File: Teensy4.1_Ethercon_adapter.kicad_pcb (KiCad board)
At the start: 2 copper layers, 20 x 32 mm, 10 parts, among them J1 Conn_01x06, J2 NE8FAV

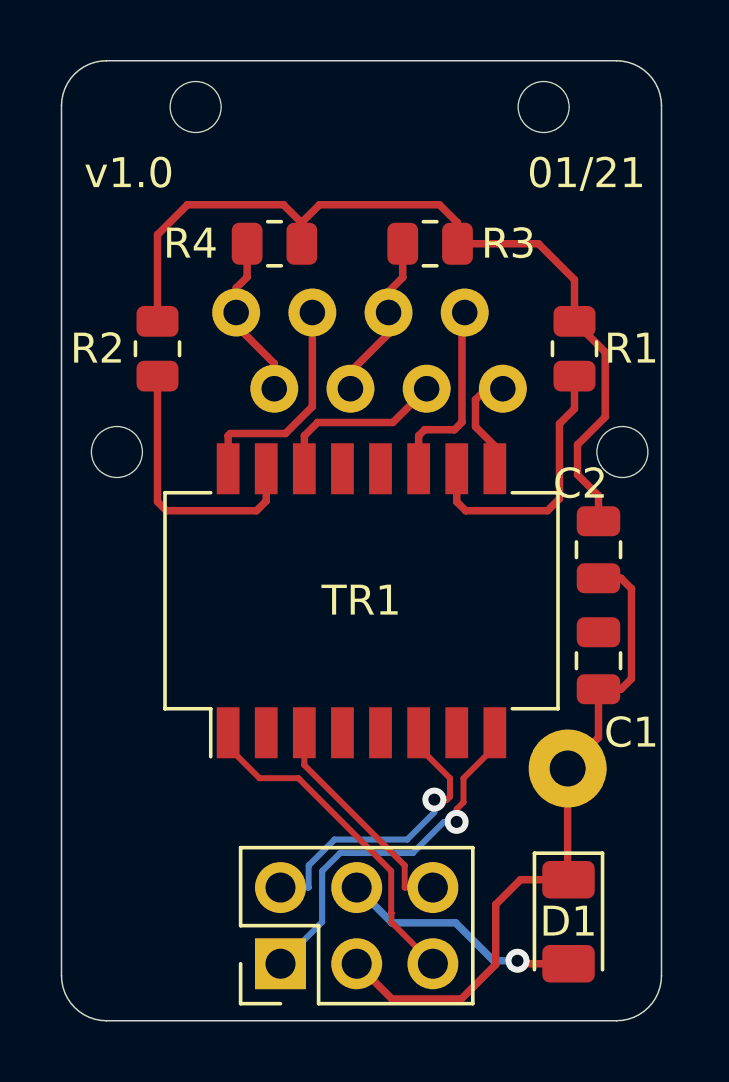
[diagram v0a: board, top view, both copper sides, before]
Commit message: Version 1.1 - fixed routing and pin header pitch (2mm)
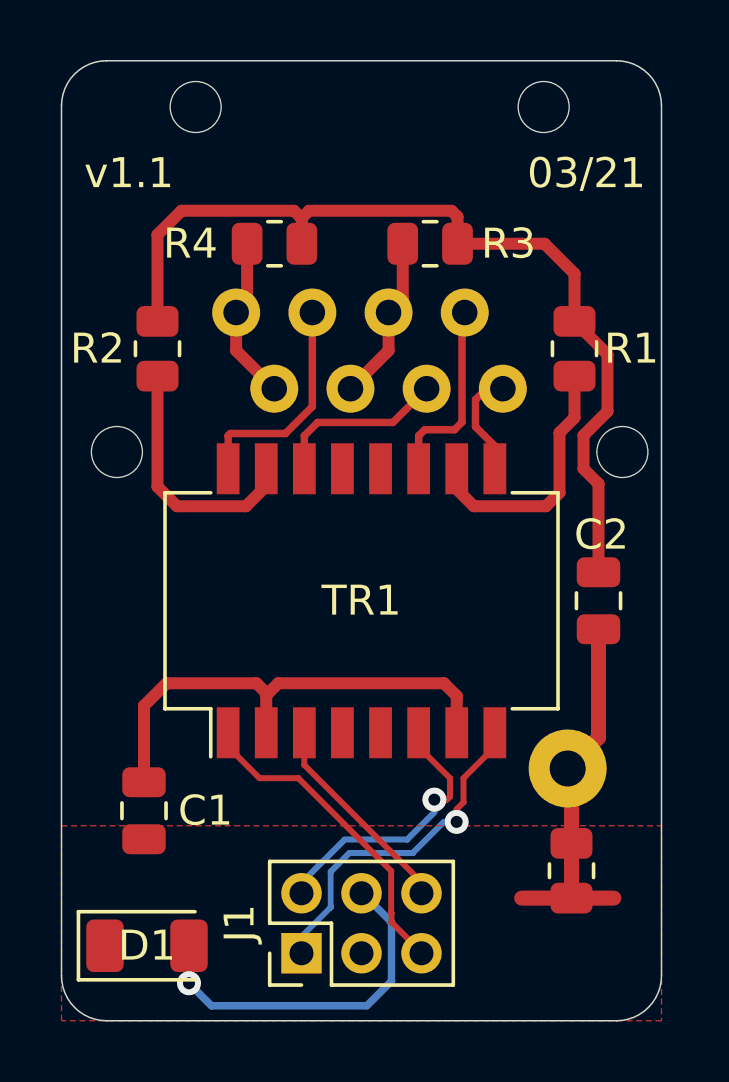
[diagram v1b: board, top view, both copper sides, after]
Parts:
- added NT1: Net-Tie_2, NetTie:NetTie-2_SMD_Pad0.5mm, F.Cu at (152.0, 110.0)
- added R5: DNP, Resistor_SMD:R_0805_2012Metric, F.Cu at (152.0, 110.0)
- J1: footprint Connector_PinHeader_2.54mm:PinHeader_2x03_P2.54mm_Vertical -> Connector_PinHeader_2.00mm:PinHeader_2x03_P2.00mm_Vertical
- moved C1 16.0 mm to (137.8, 108.0)
- moved D1 14.1 mm to (137.8, 112.5), turned to 0 degrees
- moved C2 1.70 mm to (152.9, 101.0)
- moved J1 0.78 mm to (143.0, 112.8)
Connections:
- C2 pad 2: GND -> GNDREF
- J2 pad SH: GND -> GNDREF
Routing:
- net GND: track 22.6 -> 3.33 mm
- net Net-(C1-Pad1): track 0.00 -> 16.8 mm
- net GNDREF: track 0.00 -> 7.62 mm
- net /LED: track 8.11 -> 12.3 mm
- net Net-(C2-Pad1): track 29.7 -> 31.4 mm
- net /TX+: track 12.3 -> 11.5 mm
- net /TX-: track 10.2 -> 9.36 mm
- net Net-(R2-Pad2): track 9.15 -> 8.44 mm
- added copper zone on F.Cu, net GND
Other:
- board text added: "03/21"
- board text added: "v1.1"
- board text removed: "01/21"
- board text removed: "v1.0"
